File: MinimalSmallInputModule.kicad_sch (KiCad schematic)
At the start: 17 parts, among them J1 Pogo Pins, J2 Debug Header

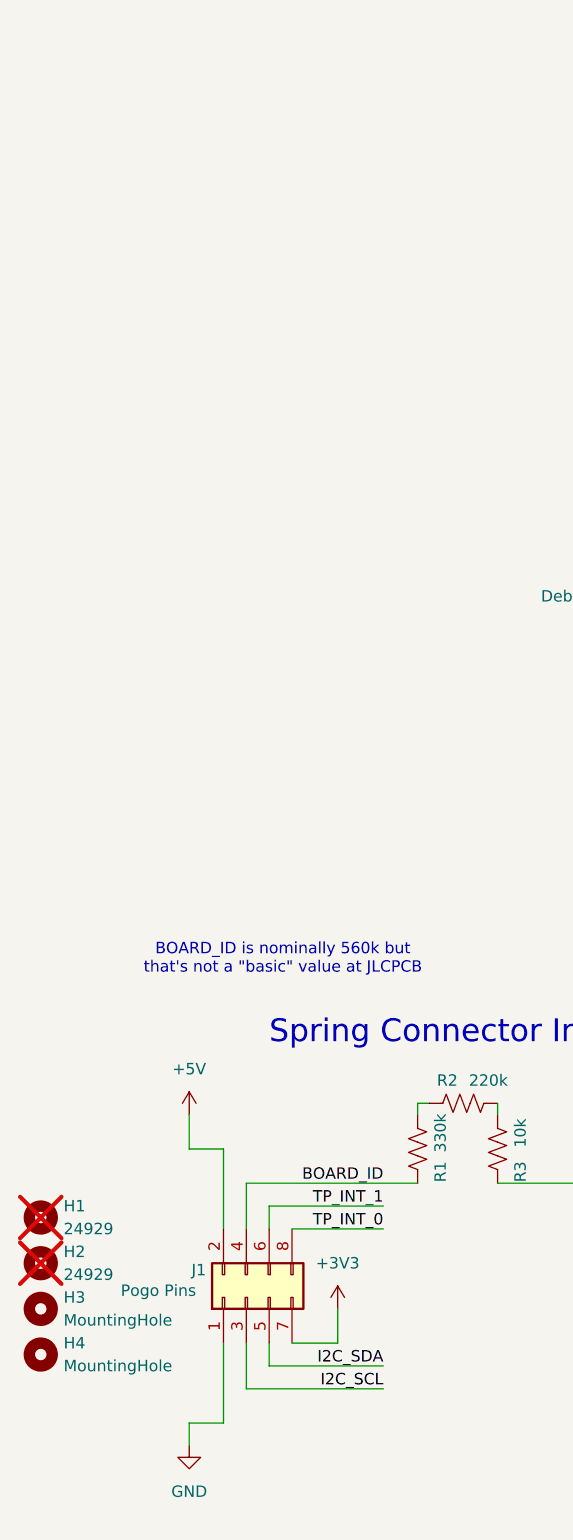
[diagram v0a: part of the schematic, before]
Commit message: First complete version sent to JLCPCB
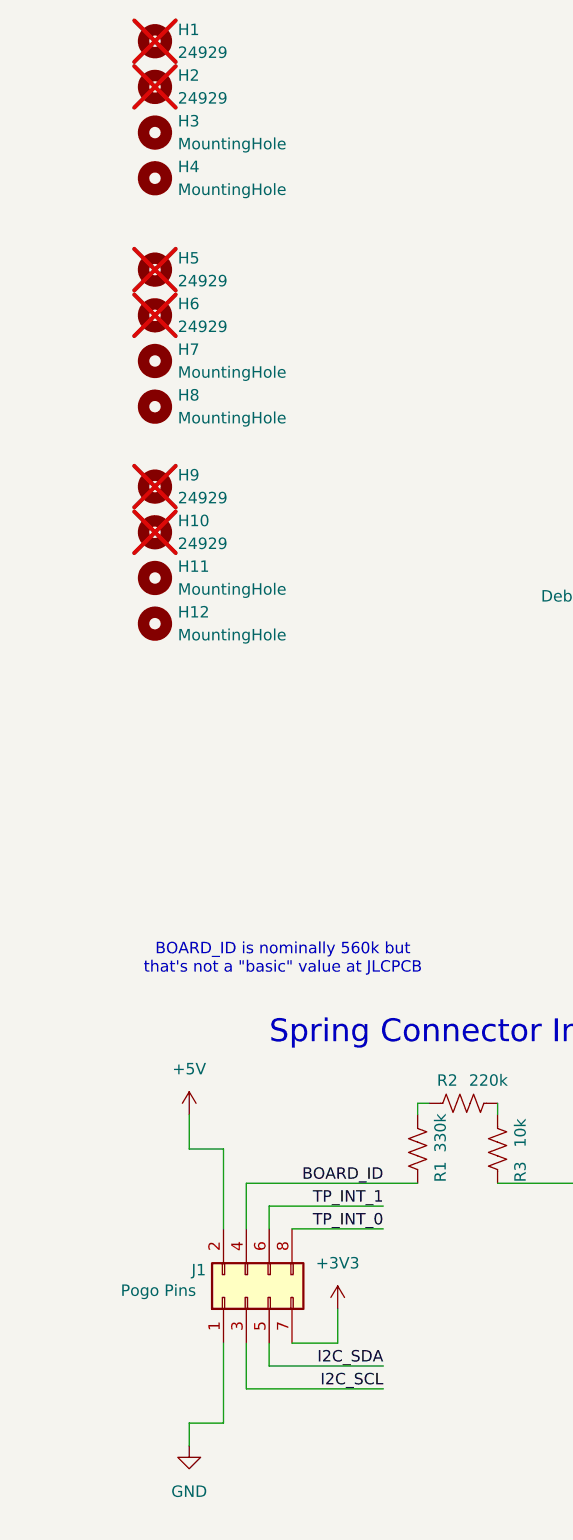
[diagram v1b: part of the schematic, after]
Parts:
- added H10, H5, H6, H9: 24929, InputModule:MountingHole_3.7mm_Pad_24929, symbol Mechanical:MountingHole
- added H11, H12, H7, H8: MountingHole, MountingHole:MountingHole_2.1mm, symbol Mechanical:MountingHole
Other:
- moved on the sheet: H1, H2, H3, H4
